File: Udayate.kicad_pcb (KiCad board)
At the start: 4 copper layers, 60.1 x 60 mm, 114 parts, among them J501 12402012E212A, J502 Conn_01x03_Pin, J503 Conn_01x03_Pin, J504 Conn_01x03_Pin, J505 Conn_01x03_Pin, J506 Conn_01x03_Pin, J507 Conn_01x03_Pin, J508 Conn_01x03_Pin, J509 Conn_01x03_Pin, J601 Conn_01x04_Socket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

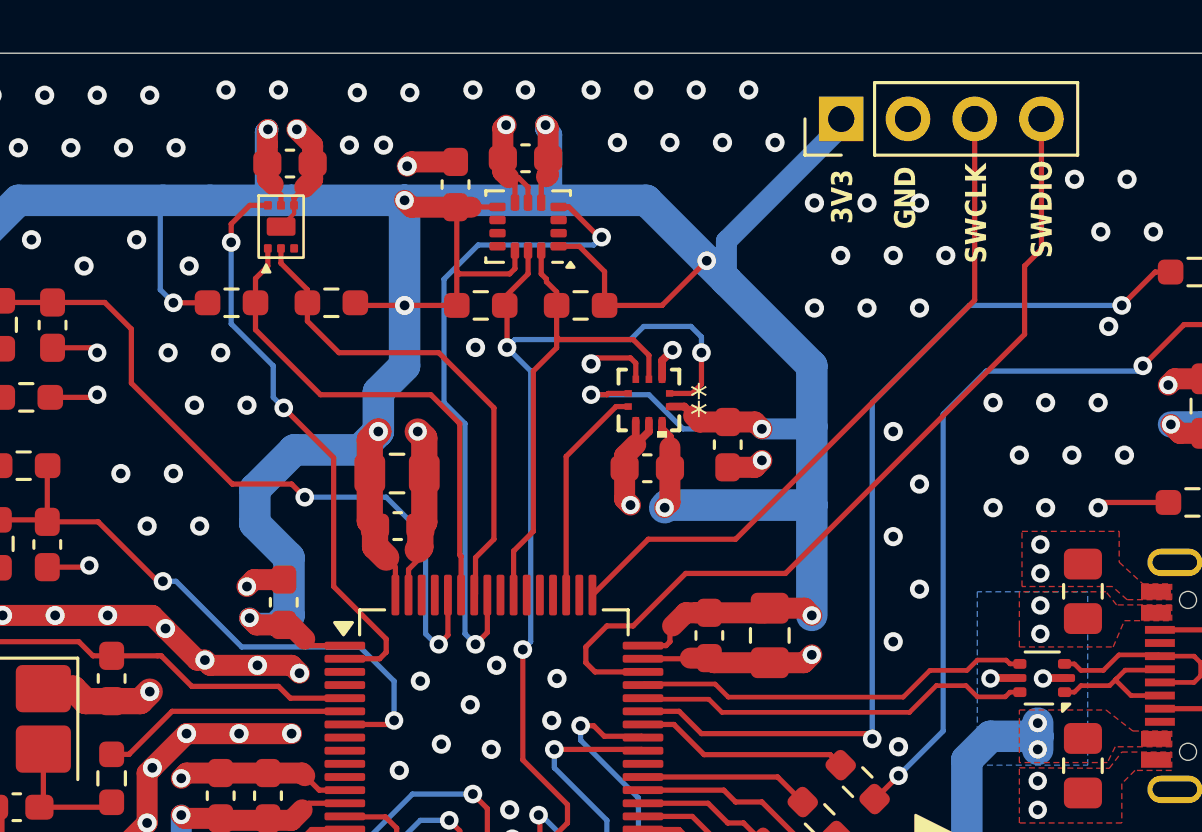
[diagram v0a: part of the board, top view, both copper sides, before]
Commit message: fix:mag & imu axis align
- change mag layout
- generate new bom
- changed rev num
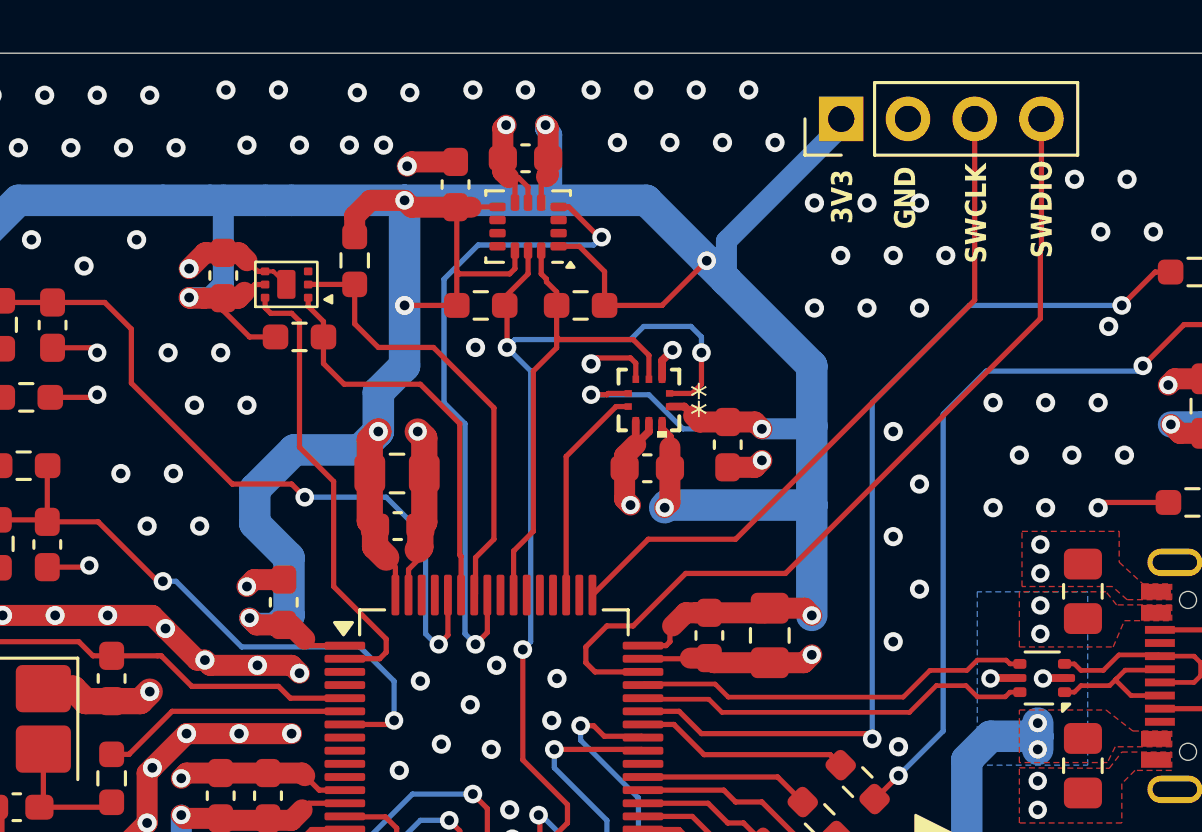
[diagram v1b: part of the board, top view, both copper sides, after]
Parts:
- moved C305 4.96 mm to (135.4, 80.5), turned to 90 degrees
- moved R222 2.90 mm to (138.3, 82.8)
- moved U303 2.21 mm to (137.8, 80.8), turned to 90 degrees
- moved R221 1.84 mm to (140.4, 79.9), turned to -90 degrees
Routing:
- net /IMUs/D_MLX90394RLD_INTB: track 22.1 -> 17.6 mm, vias 2 -> 0
- net /IMUs/D_I2C1_SDA: track 19.1 -> 15.4 mm
- net /IMUs/D_I2C1_SCL: track 19.1 -> 17.3 mm
- net +3V3: track 320.1 -> 320.5 mm, vias 23 -> 22
- net GND: vias 186 -> 187
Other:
- board text added: "Rev: 1.2.1"
- board text removed: "Rev: 1.1"
